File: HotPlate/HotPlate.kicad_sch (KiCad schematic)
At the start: 17 parts, among them J1 USB_C_Receptacle_USB2.0_14P, SW1 SW_Push, U1 RP2040, U2 USBLC6-2SC6, U3 NCP1117-3.3_SOT223, Y1 12Mhz

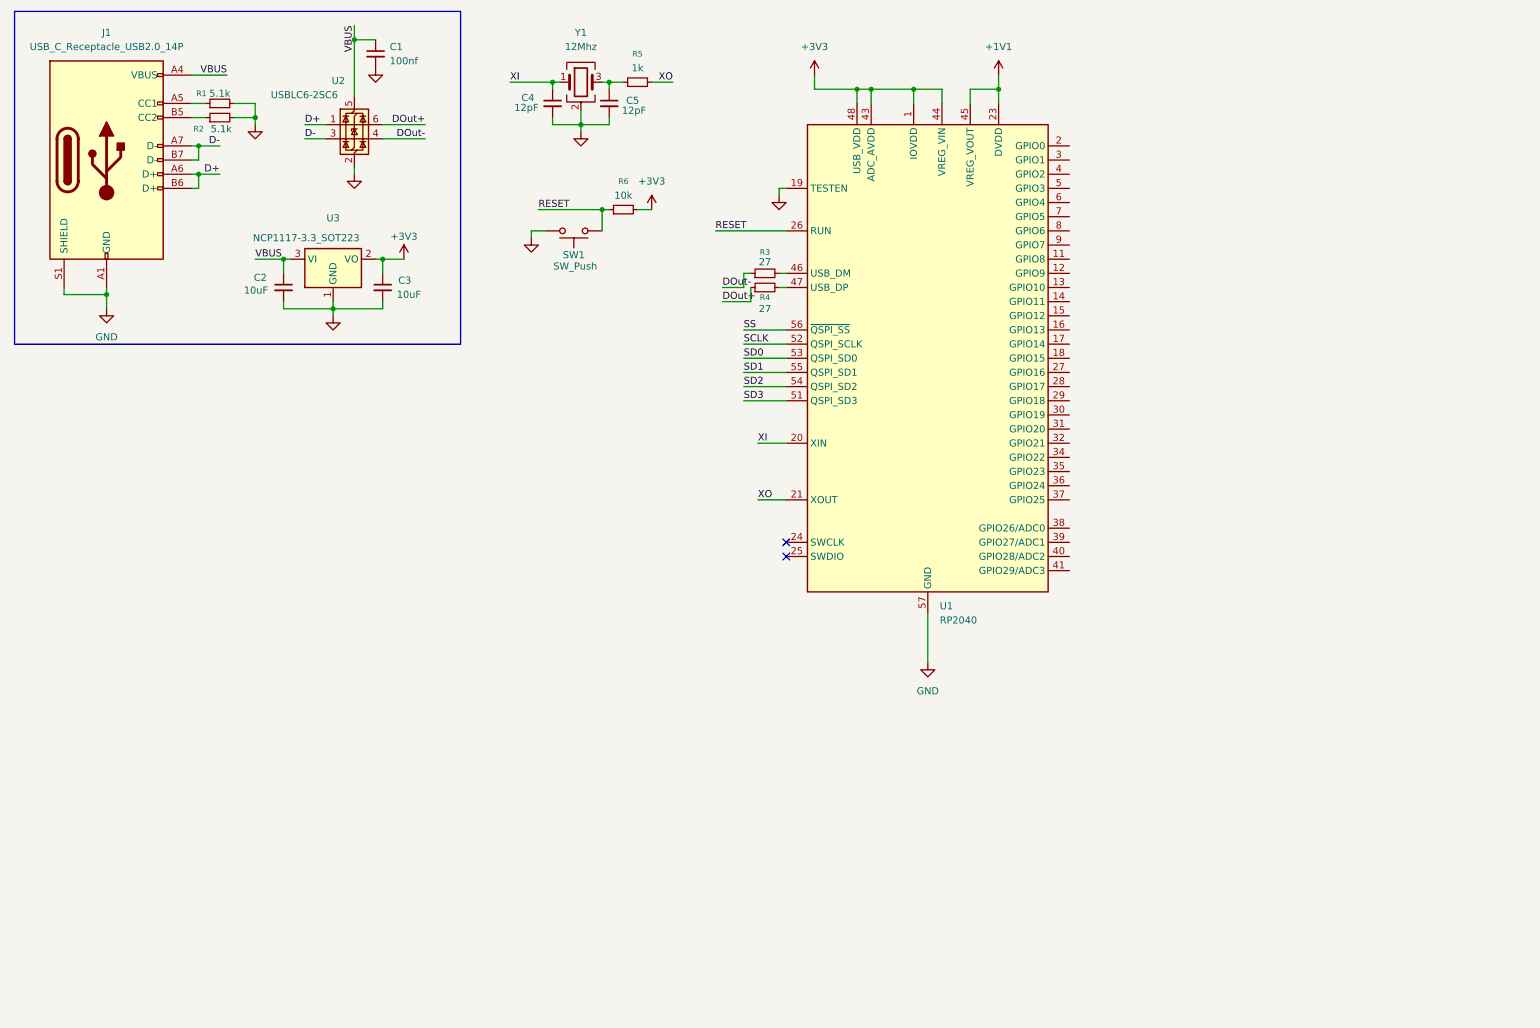
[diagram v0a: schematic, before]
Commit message: Wire up power delivery, and memory
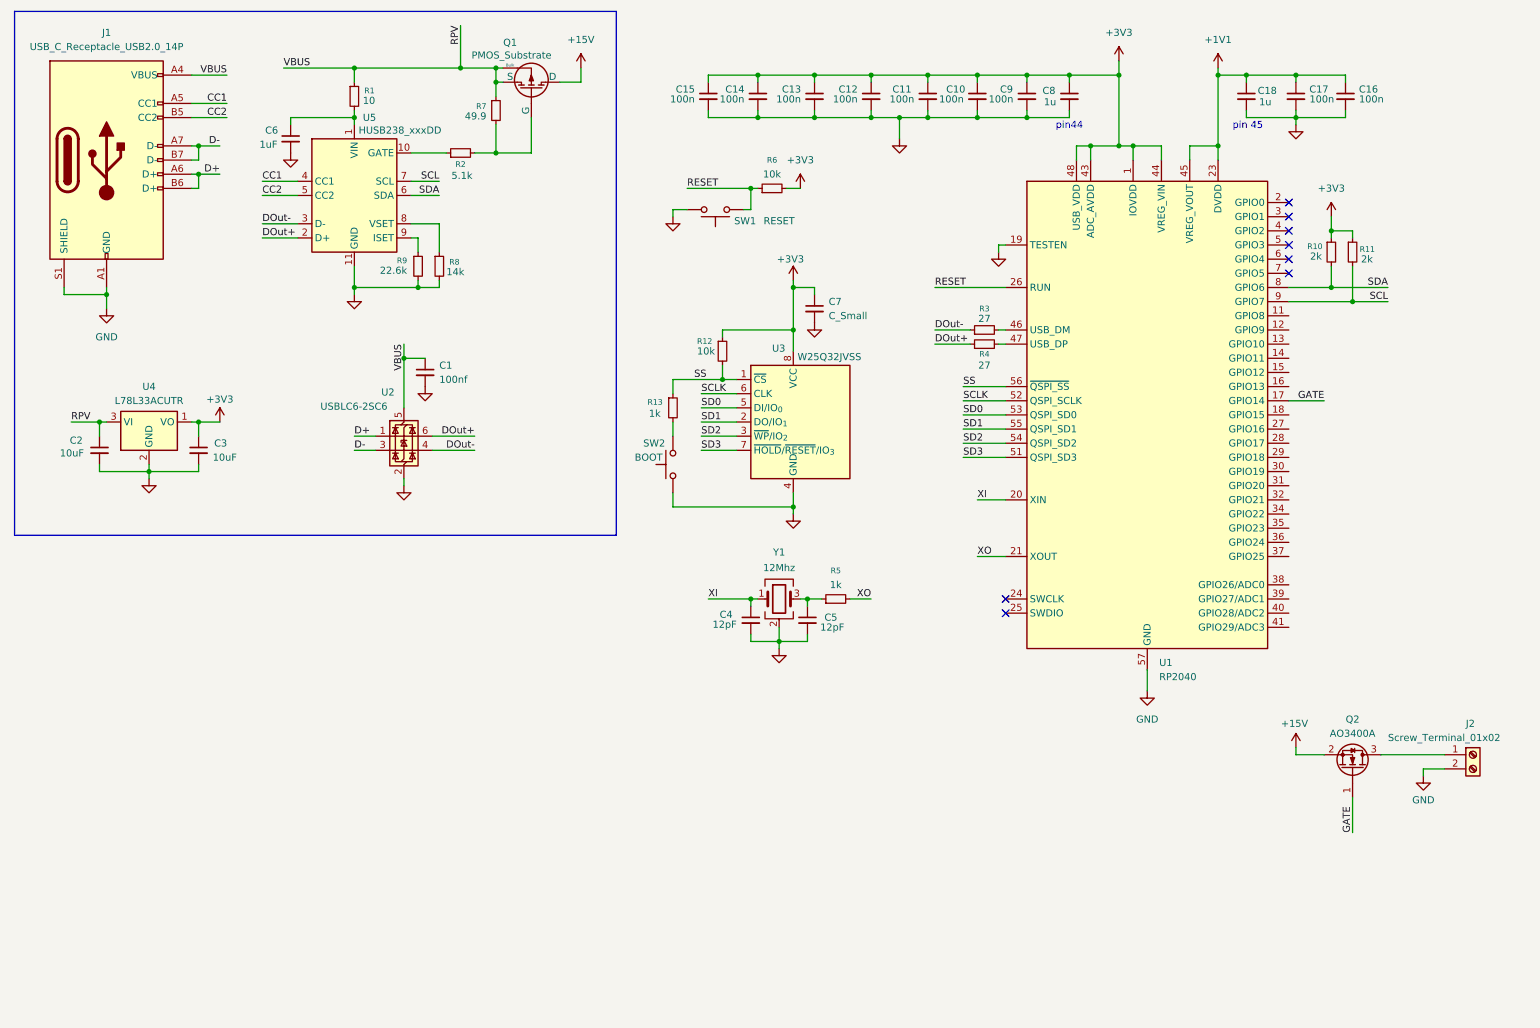
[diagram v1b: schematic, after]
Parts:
- removed U3: NCP1117-3.3_SOT223, Package_TO_SOT_SMD:SOT-223-3_TabPin2, symbol Regulator_Linear:NCP1117-3.3_SOT223
- added C10, C11, C12, C13, C14, C15, C16, C17, C9: 100n, symbol Device:C_Small
- added C18, C8: 1u, symbol Device:C_Small
- added C6: 1uF, symbol Device:C_Small
- added C7: C_Small, symbol Device:C_Small
- added J2: Screw_Terminal_01x02, symbol Connector:Screw_Terminal_01x02
- added Q1: PMOS_Substrate, symbol Simulation_SPICE:PMOS_Substrate
- added Q2: AO3400A, Package_TO_SOT_SMD:SOT-23, symbol Transistor_FET:AO3400A
- added R10, R11: 2k, symbol Device:R_Small
- added R12: 10k, symbol Device:R_Small
- added R13: 1k, symbol Device:R_Small
- added R7: 49.9, symbol Device:R_Small
- added R8: 14k, symbol Device:R_Small
- added R9: 22.6k, symbol Device:R_Small
- added SW2: BOOT, symbol Switch:SW_Push
- added U3: W25Q32JVSS, Package_SO:SOIC-8_5.3x5.3mm_P1.27mm, symbol Memory_Flash:W25Q32JVSS
- added U4: L78L33ACUTR, Package_TO_SOT_SMD:SOT-89-3, symbol Regulator_Linear:AMS1117-3.3
- added U5: HUSB238_xxxDD, Package_DFN_QFN:WDFN-10-1EP_3x3mm_P0.5mm_EP1.8x2.5mm, symbol Interface_USB:HUSB238_xxxDD
- R1: value 5.1k -> 10
- SW1: value SW_Push -> RESET
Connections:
- net +1V1: now also C16.1, C17.1, C18.1
- net +3V3: now also C10.1, C11.1, C12.1, C13.1, C14.1, C15.1, C7.1, C8.1, C9.1, R10.1, R11.1, R12.1, U3.8 (VCC), U4.1 (VO)
- net DOut+: now also U5.2 (D+)
- net DOut-: now also U5.3 (D-)
- net GND: now also C10.2, C11.2, C12.2, C13.2, C14.2, C15.2, C16.2, C17.2, C18.2, C6.2, C7.2, C8.2, C9.2, J2.2 (Pin_2), R8.2, R9.2, SW2.1, U3.4 (GND), U4.2 (GND), U5.11 (GND); no longer R1.2, R2.2
- net SCLK: now also U3.6 (CLK)
- net SD0: now also U3.5 (DI/IO_{0})
- net SD1: now also U3.2 (DO/IO_{1})
- net SD2: now also U3.3 (~{WP}/IO_{2})
- net SD3: now also U3.7 (~{HOLD}/~{RESET}/IO_{3})
- net SS: now also R12.2, R13.1, U3.1 (~{CS})
- net at R2.1: now also U5.10 (GATE); no longer J1.B5 (CC2)
- net CC1: now reaches J1.A5 (CC1)
- net CC1: now also U5.4 (CC1); no longer R1.1
- net GATE: now reaches U1.17 (GPIO14)
- net GATE: now also Q2.1 (G)
- net SDA: now reaches U1.8 (GPIO6)
- net SDA: now also R10.2, U5.6 (SDA)
- net SCL: now reaches U1.9 (GPIO7)
- net SCL: now also R11.2, U5.7 (SCL)
- net VBUS renamed RPV
- net RPV: now also R1.1, Q1.3 (S), Q1.4 (Bulk), R7.1, U4.3 (VI)
- new net: C6.1, R1.2, U5.1 (VIN)
- new net: Q1.2 (G), R2.2, R7.2
- new net: R9.1, U5.9 (ISET)
- new net: J2.1 (Pin_1), Q2.3 (D)
- new net: R8.1, U5.8 (VSET)
- new net: R13.2, SW2.2
- new net +15V: Q1.1 (D), Q2.2 (S)
- new net CC2: J1.B5 (CC2), U5.5 (CC2)
- no-connect marks 2 -> 8
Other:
- note added: "pin 45"
- note added: "pin44"
- moved on the sheet: C1, C2, C3, C4, C5, R3, R4, R5, R6, SW1, U1, U2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

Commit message: Wire up power delivery, and memory
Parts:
- added R14: 10k, symbol Device:R_Small
- added R15: 100, symbol Device:R_Small
- J2: value Screw_Terminal_01x02 -> Heater
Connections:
- net GATE: now also R14.1, R15.2; no longer U1.17 (GPIO14)
- net GND: now also R14.2
- new net: R15.1, U1.17 (GPIO14)
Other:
- moved on the sheet: J2, Q2

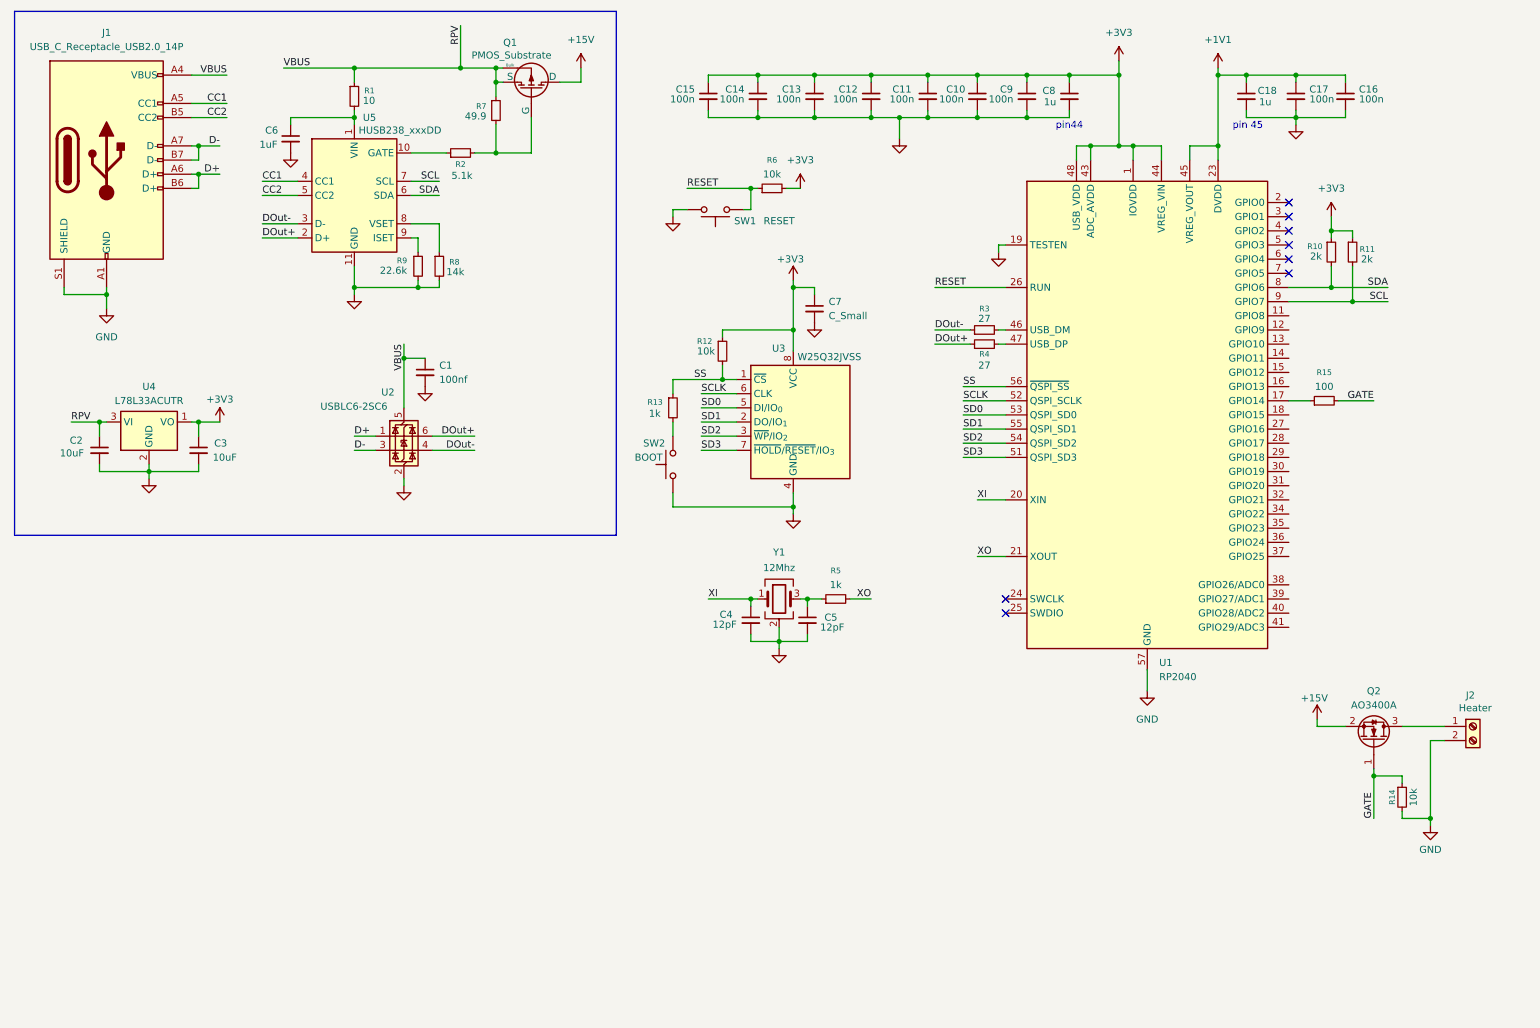
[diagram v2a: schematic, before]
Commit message: Re-add buttons and add thermistor
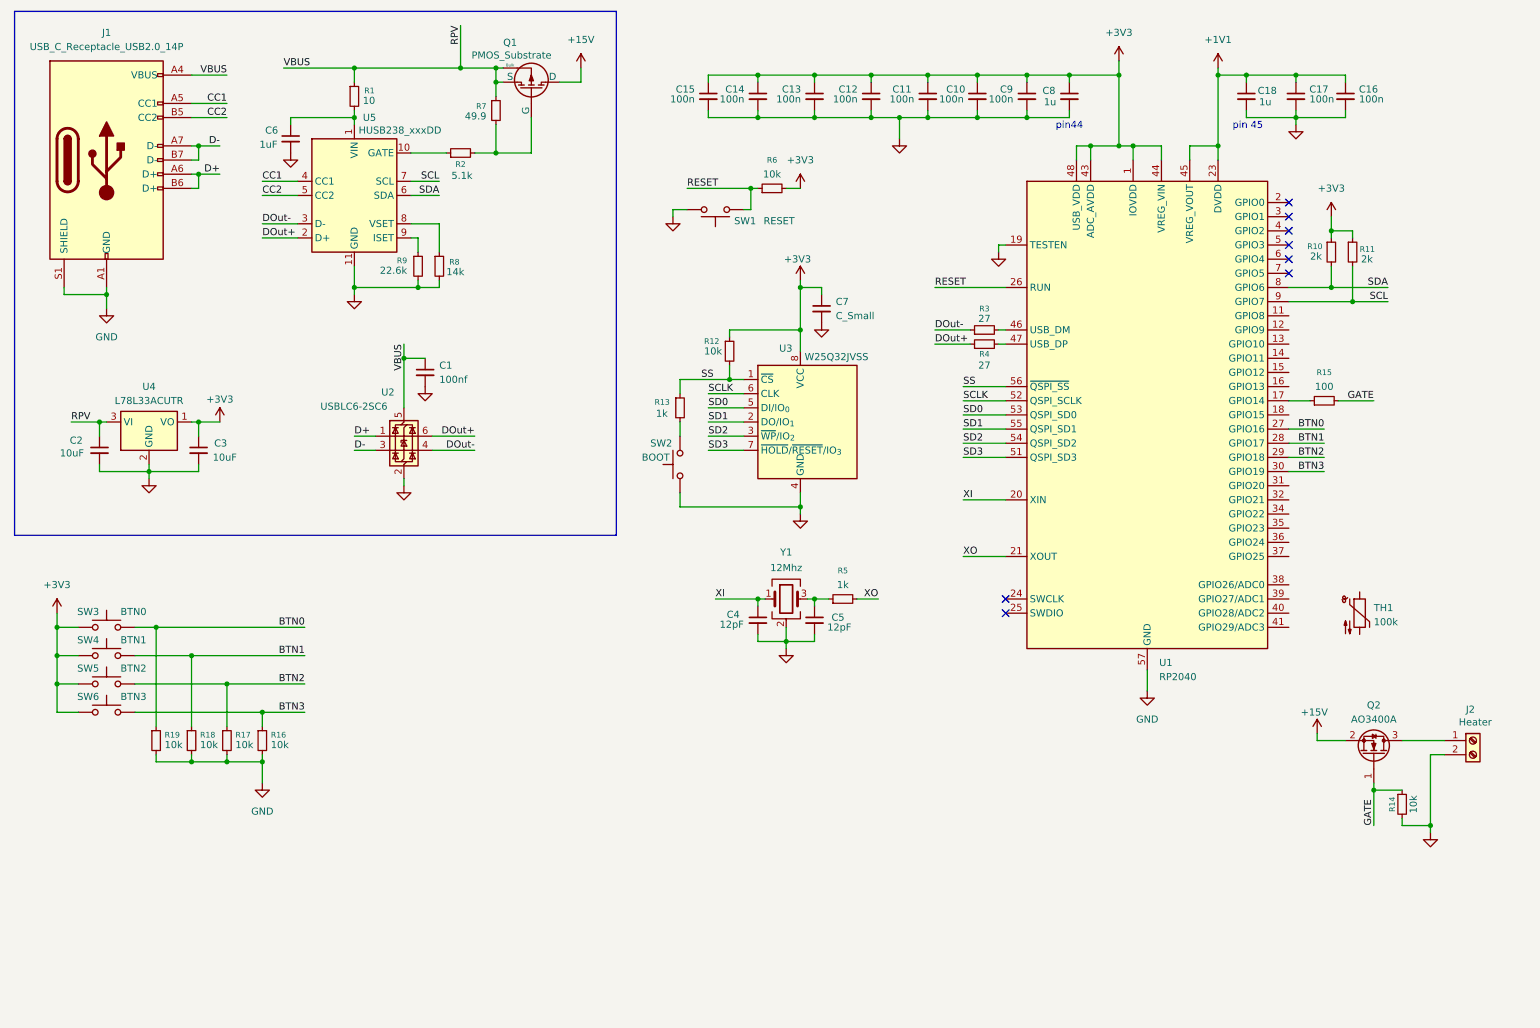
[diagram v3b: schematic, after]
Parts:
- added R16, R17, R18, R19: 10k, symbol Device:R_Small
- added SW3: BTN0, symbol Switch:SW_Push
- added SW4: BTN1, symbol Switch:SW_Push
- added SW5: BTN2, symbol Switch:SW_Push
- added SW6: BTN3, symbol Switch:SW_Push
- added TH1: 100k, symbol Device:Thermistor_NTC
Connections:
- net +3V3: now also SW3.1, SW4.1, SW5.1, SW6.1
- net GND: now also R16.2, R17.2, R18.2, R19.2
- net BTN0: now reaches U1.27 (GPIO16)
- net BTN0: now also R19.1, SW3.2
- net BTN1: now reaches U1.28 (GPIO17)
- net BTN1: now also R18.1, SW4.2
- net BTN2: now reaches U1.29 (GPIO18)
- net BTN2: now also R17.1, SW5.2
- net BTN3: now reaches U1.30 (GPIO19)
- net BTN3: now also R16.1, SW6.2
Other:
- moved on the sheet: C4, C5, C7, J2, Q2, R12, R13, R14, R5, SW2, U3, Y1

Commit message: Wire Buttons, screen, thermistor, fuse
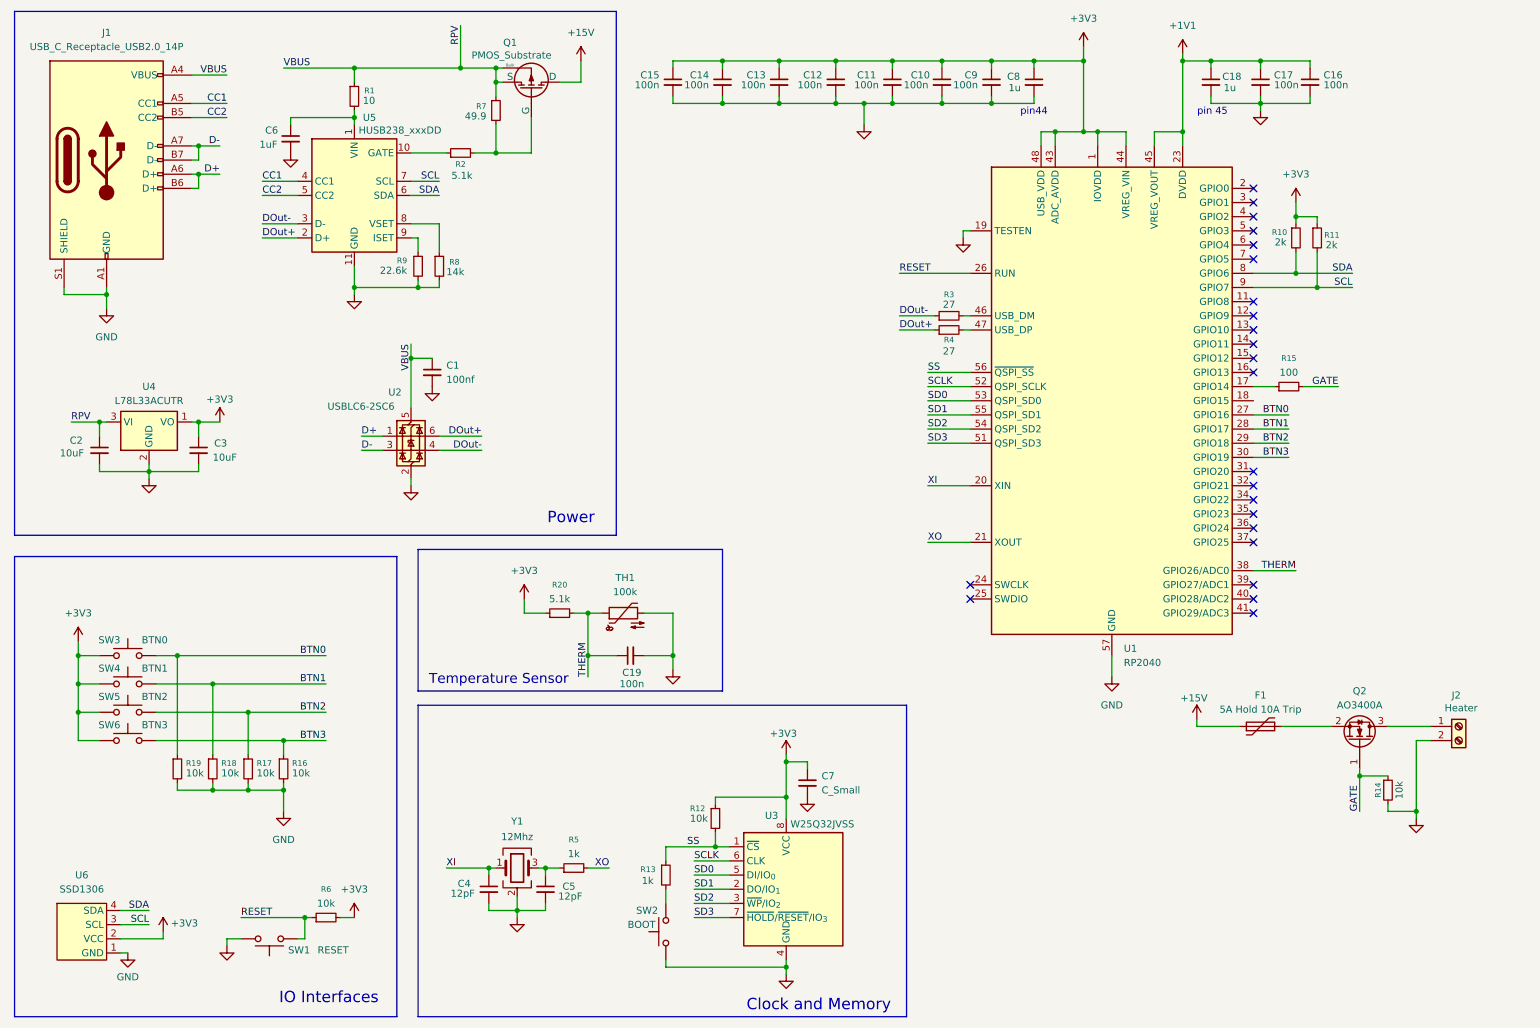
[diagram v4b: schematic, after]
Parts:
- added C19: 100n, symbol Device:C_Small
- added F1: 5A Hold 10A Trip, symbol Device:Polyfuse
- added R20: 5.1k, symbol Device:R_Small
- added U6: SSD1306, symbol Screen:SSD1306
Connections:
- net +15V: now also F1.1; no longer Q2.2 (S)
- net +3V3: now also R20.1, U6.2 (VCC)
- net GND: now also TH1.2, C19.2, U6.1 (GND)
- net SCL: now also U6.3 (SCL)
- net SDA: now also U6.4 (SDA)
- net THERM: now reaches TH1.1
- net THERM: now also U1.38 (GPIO26/ADC0), C19.1, R20.2
- new net: F1.2, Q2.2 (S)
- no-connect marks 8 -> 23
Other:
- note added: "Clock and Memory"
- note added: "IO Interfaces"
- note added: "Power"
- note added: "Temperature Sensor"
- moved on the sheet: C1, C10, C11, C12, C13, C14, C15, C16, C17, C18, C4, C5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
